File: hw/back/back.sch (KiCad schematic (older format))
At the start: 0 parts

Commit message: added first schematic protitype
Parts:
- added BT?: 2XLP7836140, symbol Device:Battery
- added C? (x2): 4u7, symbol Device:CP
- added C?: 100n, symbol Device:C
- added C? (x3): CP, symbol Device:CP
- added C?: C, symbol Device:C
- added C?: 1u, symbol Device:C
- added C?: 6u8, symbol Device:C
- added C?: 47n, symbol Device:C
- added C? (x2): 10u, symbol Device:C
- added C?: 4n7, symbol Device:C
- added D? (x3): LED, symbol Device:LED
- added D? (x3): D_Schottky, symbol Device:D_Schottky
- added J? (x2): POWER, symbol Connector_Generic:Conn_01x02
- added L?: L, symbol Device:L
- added L?: 2u2, symbol Device:L
- added Q?: Q_PNP_BCE, symbol Device:Q_PNP_BCE
- added Q?: Q_NMOS_DGS, symbol Device:Q_NMOS_DGS
- added R?: 10m, symbol Device:R
- added R? (x7): R, symbol Device:R
- added R? (x2): 2k2, symbol Device:R
- added R?: 180R, symbol Device:R
- added R? (x5): 10k, symbol Device:R
- added TH?: Thermistor_NTC, symbol Device:Thermistor_NTC
- added U?: LTC4150, Package_SO:MSOP-10_3x3mm_P0.5mm, symbol KLIB_Battery:LTC4150
- added U?: BQ2057CSN, Package_SO:SOIC-8_3.9x4.9mm_P1.27mm, symbol KLIB_Battery:BQ2057CSN
- added U?: LTC1871, Package_SO:MSOP-10_3x3mm_P0.5mm, symbol KLIB_Regul:LTC1871
- added U?: BQ24192, Package_DFN_QFN:QFN-24-1EP_4x4mm_P0.5mm_EP2.6x2.6mm, symbol KLIB_Battery:BQ24192
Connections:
- net labels added: +3V3, +5V5, +BATT, ADAPTER, BATT_CELL, GND, INT, POL, SCL, SDA, VCC, ~INT, ~SHDN
- wire segments 0 -> 142
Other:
- note added: "PSEL\n L: ADAPTER\n H: USB\n"
- note added: "~CE\n Charge Enable"

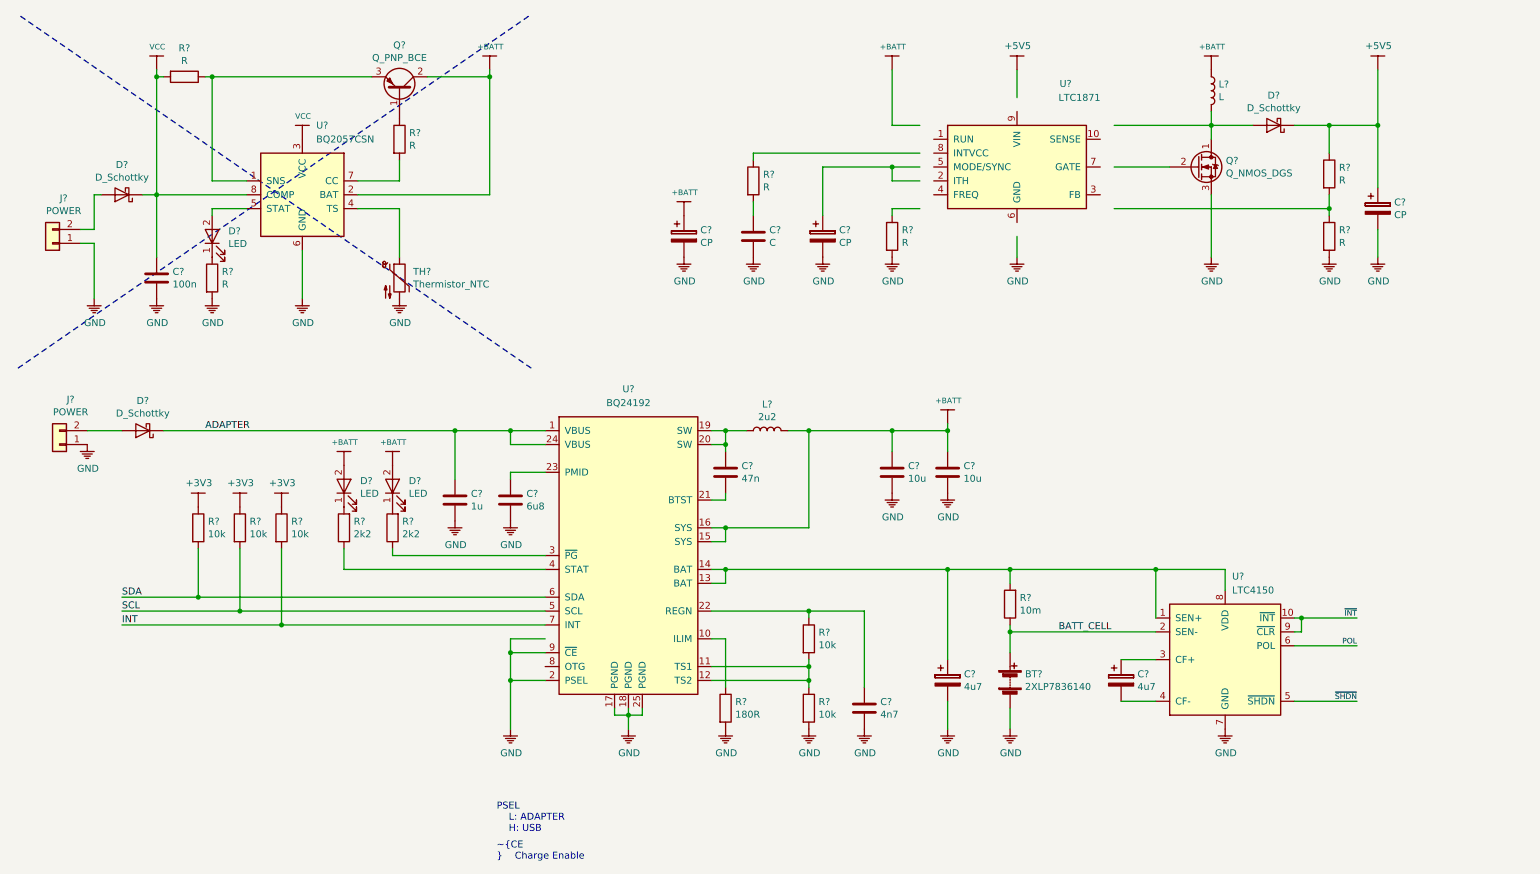
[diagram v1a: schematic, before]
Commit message: updated schematic, select components
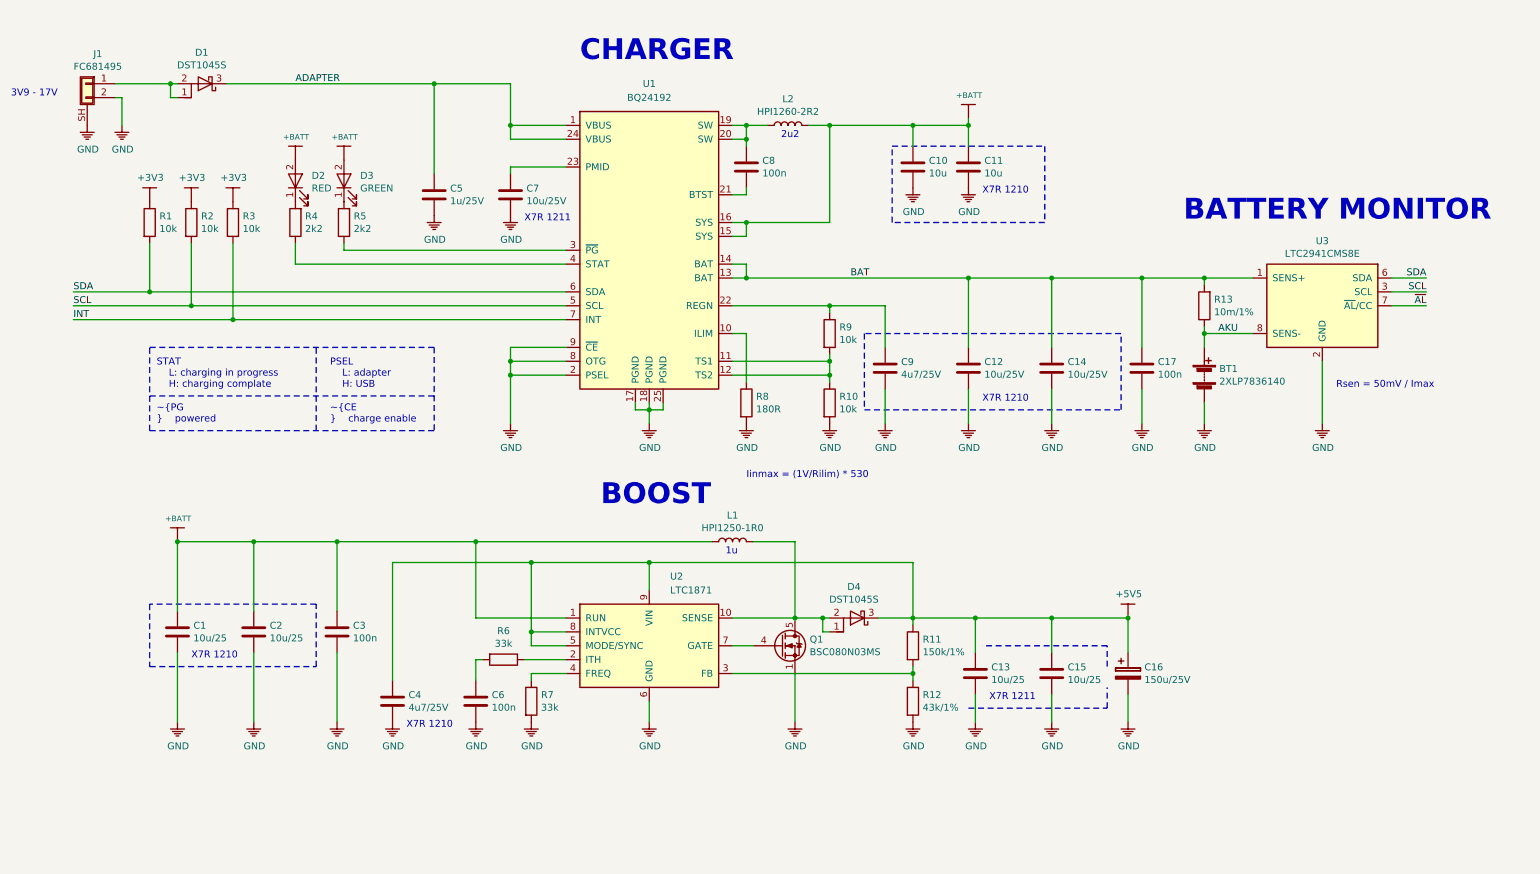
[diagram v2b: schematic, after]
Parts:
- removed C? (x2): 4u7, symbol Device:CP
- removed C?: 100n, symbol Device:C
- removed C? (x2): CP, symbol Device:CP
- removed D?: LED, symbol Device:LED
- removed D? (x3): D_Schottky, symbol Device:D_Schottky
- removed J? (x2): POWER, symbol Connector_Generic:Conn_01x02
- removed L?: L, symbol Device:L
- removed Q?: Q_PNP_BCE, symbol Device:Q_PNP_BCE
- removed Q?: Q_NMOS_DGS, symbol Device:Q_NMOS_DGS
- removed R? (x4): R, symbol Device:R
- removed TH?: Thermistor_NTC, symbol Device:Thermistor_NTC
- removed U?: LTC4150, Package_SO:MSOP-10_3x3mm_P0.5mm, symbol KLIB_Battery:LTC4150
- removed U?: BQ2057CSN, Package_SO:SOIC-8_3.9x4.9mm_P1.27mm, symbol KLIB_Battery:BQ2057CSN
- removed U?: LTC1871, Package_SO:MSOP-10_3x3mm_P0.5mm, symbol KLIB_Regul:LTC1871
- added C1, C13, C15, C2: 10u/25, symbol Device:C
- added C12, C14: 10u/25V, symbol Device:C
- added C17, C3: 100n, symbol Device:C
- added C4: 4u7/25V, symbol Device:C
- added D1, D4: DST1045S, Package_TO_SOT_SMD:TO-277B, symbol Device:D_Schottky_AAK
- added J1: FC681495, symbol Connector_Generic_Shielded:Conn_01x02_Shielded
- added L1: HPI1250-1R0, symbol Device:L
- added Q1: BSC080N03MS, Package_TO_SOT_SMD:TDSON-8-1, symbol Transistor_FET:BSC082N10LSG
- added R6: 33k, symbol Device:R
- added U2: LTC1871, Package_SO:MSOP-10_3x3mm_P0.5mm, symbol KLIB_Regul:LTC1871
- added U3: LTC2941CMS8E, Package_SO:MSOP-8-1EP_3x3mm_P0.65mm_EP1.68x1.88mm, symbol KLIB_Battery:LTC2941CMS8E
- C16: renamed from C?; value CP -> 150u/25V
- C5: renamed from C?; value 1u -> 1u/25V
- C6: renamed from C?; value C -> 100n
- C7: renamed from C?; value 6u8 -> 10u/25V
- C8: renamed from C?; value 47n -> 100n
- C9: renamed from C?; value 4n7 -> 4u7/25V
- D2: renamed from D?; value LED -> RED
- D3: renamed from D?; value LED -> GREEN
- L2: renamed from L?; value 2u2 -> HPI1260-2R2
- R11: renamed from R?; value R -> 150k/1%
- R12: renamed from R?; value R -> 43k/1%
- R13: renamed from R?; value 10m -> 10m/1%
- R7: renamed from R?; value R -> 33k
- gave numbers to parts that had none: 12
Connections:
- net labels added: AKU, BAT, ~AL
- net labels removed: BATT_CELL, POL, VCC, ~INT, ~SHDN
- wire segments 142 -> 144
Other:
- note added: "1u"
- note added: "2u2"
- note added: "3V9 - 17V"
- note added: "BATTERY MONITOR"
- note added: "BOOST"
- note added: "CHARGER"
- note added: "Iinmax = (1V/Rilim) * 530"
- note added: "PSEL\n L: adapter\n H: USB\n"
- note added: "Rsen = 50mV / Imax"
- note added: "STAT\n L: charging in progress\n H: charging complate"
- note added: "X7R 1210"
- note added: "X7R 1211"
- note added: "~CE\n charge enable"
- note added: "~PG\n powered"
- note removed: "PSEL\n L: ADAPTER\n H: USB\n"
- note removed: "~CE\n Charge Enable"
- moved on the sheet: BT1, C10, C11, C16, C5, C6, C7, C8, C9, D2, D3, L2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

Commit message: updated schematic, completed charger and created hierarchial  list for charger
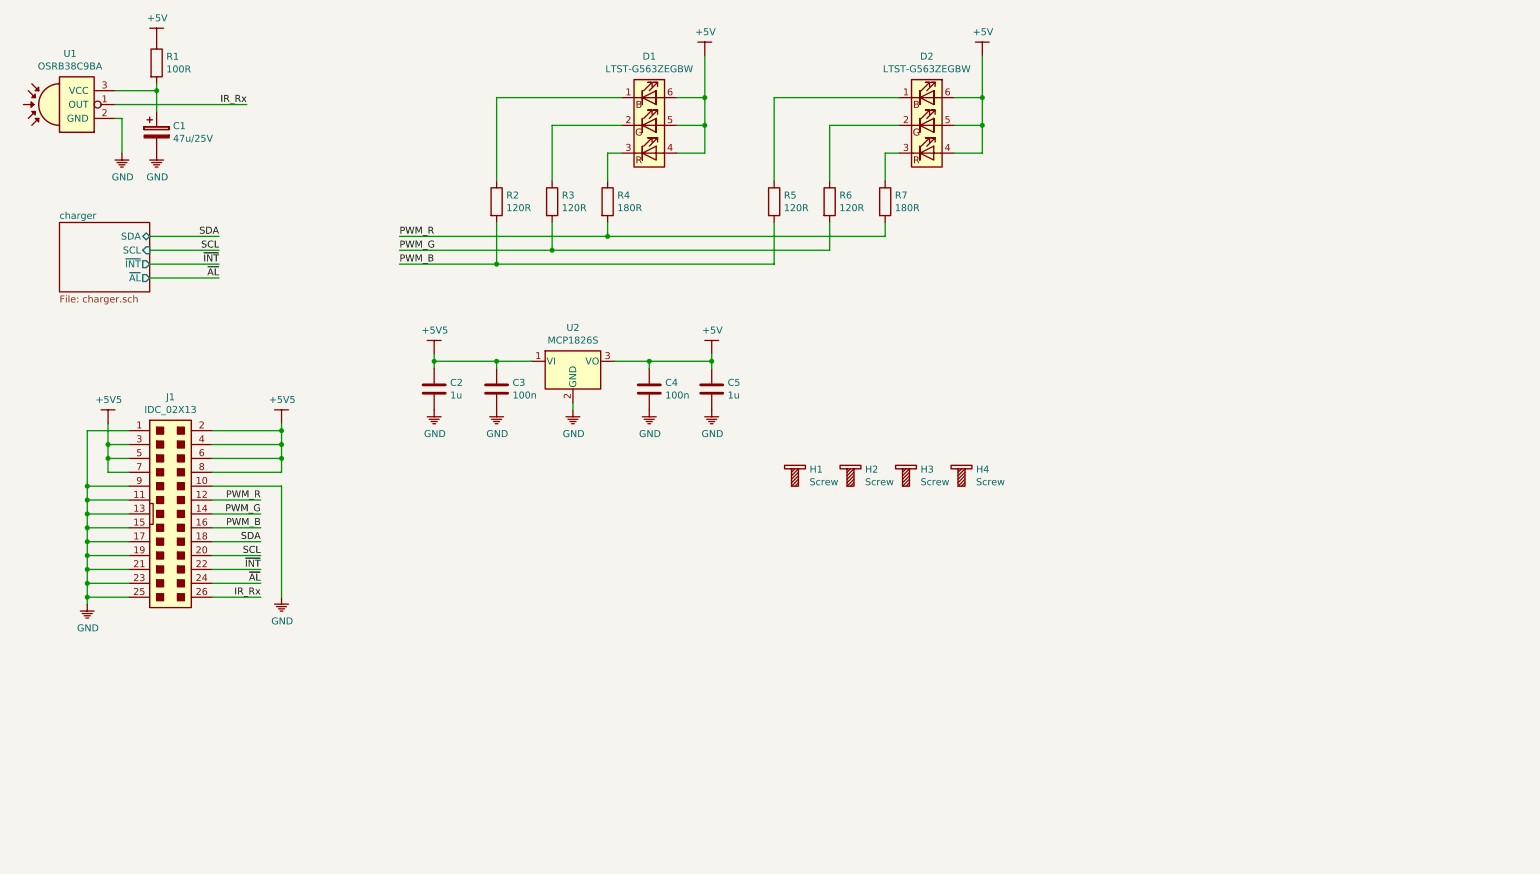
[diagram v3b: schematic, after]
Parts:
- removed BT1: 2XLP7836140, symbol Device:Battery
- removed C1, C13, C15: 10u/25, symbol Device:C
- removed C10, C11: 10u, symbol Device:C
- removed C12, C14, C7: 10u/25V, symbol Device:C
- removed C16: 150u/25V, symbol Device:CP
- removed C17, C6, C8: 100n, symbol Device:C
- removed C9: 4u7/25V, symbol Device:C
- removed D1, D4: DST1045S, Package_TO_SOT_SMD:TO-277B, symbol Device:D_Schottky_AAK
- removed D2: RED, symbol Device:LED
- removed D3: GREEN, symbol Device:LED
- removed J1: FC681495, symbol Connector_Generic_Shielded:Conn_01x02_Shielded
- removed L1: HPI1250-1R0, symbol Device:L
- removed L2: HPI1260-2R2, symbol Device:L
- removed Q1: BSC080N03MS, Package_TO_SOT_SMD:TDSON-8-1, symbol Transistor_FET:BSC082N10LSG
- removed R10, R9: 10k, symbol Device:R
- removed R11: 150k/1%, symbol Device:R
- removed R12: 43k/1%, symbol Device:R
- removed R13: 10m/1%, symbol Device:R
- removed R8: 180R, symbol Device:R
- removed U1: BQ24192, Package_DFN_QFN:QFN-24-1EP_4x4mm_P0.5mm_EP2.6x2.6mm, symbol KLIB_Battery:BQ24192
- removed U2: LTC1871, Package_SO:MSOP-10_3x3mm_P0.5mm, symbol KLIB_Regul:LTC1871
- removed U3: LTC2941CMS8E, Package_SO:MSOP-8-1EP_3x3mm_P0.65mm_EP1.68x1.88mm, symbol KLIB_Battery:LTC2941CMS8E
- added C1: 47u/25V, symbol Device:CP
- added D1, D2: LTST-G563ZEGBW, LEDs:LED_WS2812-PLCC6, symbol KLIB_Opto:LTST-G563ZEGBW
- added H1, H2, H3, H4: Screw, wyk_mech:screw_M3, symbol KLIB_Mech:Screw
- added J1: IDC_02X13, Connectors:IDC_Header_Straight_26pins, symbol KLIB_Con_IDC:IDC_02X13
- added U1: OSRB38C9BA, symbol KLIB_Opto:OSRB38C9BA
- added U2: MCP1826S, Package_TO_SOT_SMD:SOT-223-3_TabPin2, symbol Regulator_Linear:MCP1826S
- C2: value 10u/25 -> 1u
- C4: value 4u7/25V -> 100n
- C5: value 1u/25V -> 1u
- R1: value 10k -> 100R
- R2, R3: value 10k -> 120R
- R4: value 2k2 -> 180R
- R5: value 2k2 -> 120R
- R6: value 33k -> 120R
- R7: value 33k -> 180R
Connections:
- net +BATT is gone; now on net +5V5: C2.1, C3.1
- net INT is gone; now on net PWM_G: R3.2
- net +5V5: now also J1.2, J1.3, J1.4, J1.5, J1.6, J1.7, J1.8, U2.1 (VI); no longer C4.1
- net GND: now also C1.2, J1.1, J1.10, J1.11, J1.13, J1.15, J1.17, J1.19, J1.21, J1.23, J1.25, J1.9, U1.2 (GND), U2.2 (GND); no longer R7.2
- net SCL: now also J1.20; no longer R2.2
- net SDA: now also J1.18; no longer R1.2
- net ~AL: now also J1.24
- net at R7.1: now also D2.3 (BK)
- net PWM_G: now reaches R6.2
- net PWM_G: now also J1.14
- net at R5.1: now also D2.1 (RK)
- net at R4.1: now also D1.3 (BK)
- net PWM_R: now reaches R4.2
- net PWM_R: now also R7.2, J1.12
- net PWM_B: now reaches R5.2
- net PWM_B: now also R2.2, J1.16
- net at R6.1: now also D2.2 (GK)
- removed net +3V3: R1.1, R2.1, R3.1
- net ADAPTER renamed +5V
- net +5V: now also C4.1, R1.1, D1.4 (BA), D1.5 (GA), D1.6 (RA), D2.4 (BA), D2.5 (GA), D2.6 (RA), U2.3 (VO)
- new net: D1.1 (RK), R2.1
- new net: D1.2 (GK), R3.1
- new net: C1.1, R1.2, U1.3 (VCC)
- new net IR_Rx: J1.26, U1.1 (OUT)
- new net ~INT: J1.22
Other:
- note removed: "1u"
- note removed: "2u2"
- note removed: "3V9 - 17V"
- note removed: "BATTERY MONITOR"
- note removed: "BOOST"
- note removed: "CHARGER"
- note removed: "Iinmax = (1V/Rilim) * 530"
- note removed: "PSEL\n L: adapter\n H: USB\n"
- note removed: "Rsen = 50mV / Imax"
- note removed: "STAT\n L: charging in progress\n H: charging complate"
- note removed: "X7R 1210"
- note removed: "X7R 1211"
- note removed: "~CE\n charge enable"
- note removed: "~PG\n powered"
